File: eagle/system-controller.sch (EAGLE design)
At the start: 226 parts, among them J1 1, Q1 MOSFET-P-N-PAIR, Q10 MOSFET-P-N-PAIR, Q11 DNP/NTR4101P, Q2 MOSFET-P-N-PAIR, Q3 DON3035L, Q4 MOSFET-P-N-PAIR, Q5 MOSFET-P-N-PAIR, Q6 MOSFET-P-N-PAIR, Q7 MOSFET-P-N-PAIR, Q8 MOSFET-P-N-PAIR, Q9 DNP/NTR4101P, U1 TPS25944LRVCRWQFN-20-3X4, U10 TPS25944LRVCRWQFN-20-3X4, U11 ACPL-M61L, U12 ACPL-M61L, U13 TPS25944LRVCRWQFN-20-3X4, U14 ACPL-M61L, U15 ACPL-M61L, U2 LP5907MFX-3.0, U3 TPS25944LRVCRWQFN-20-3X4, U4 TPS25944LRVCRWQFN-20-3X4, U5 TPS25944LRVCRWQFN-20-3X4, U6 TPS25944LRVCRWQFN-20-3X4, U7 ATMEGA128L-8A(U/N), U8 TS4100, U9 TPS25944LRVCRWQFN-20-3X4, X1 8 MHz CRYSTAL-ABRACON-ABM3-SMD

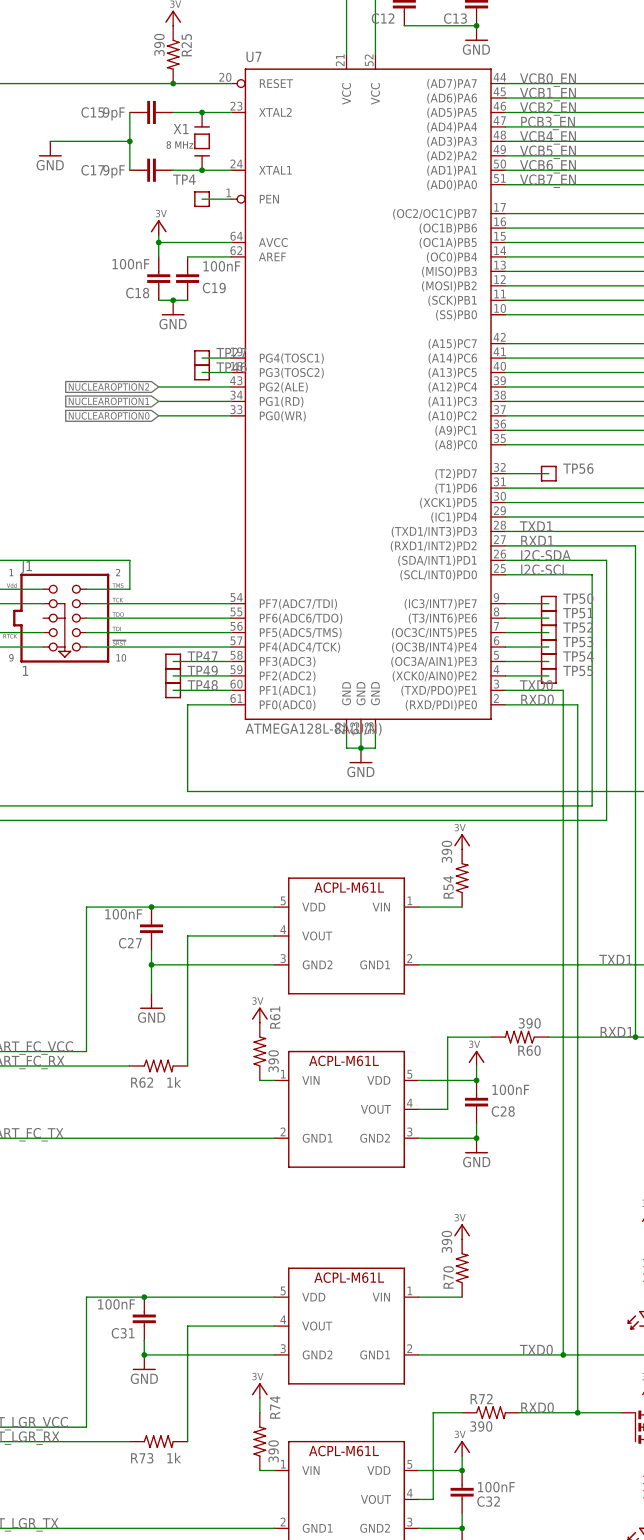
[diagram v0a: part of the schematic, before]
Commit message: Updating resitor and capacitor names
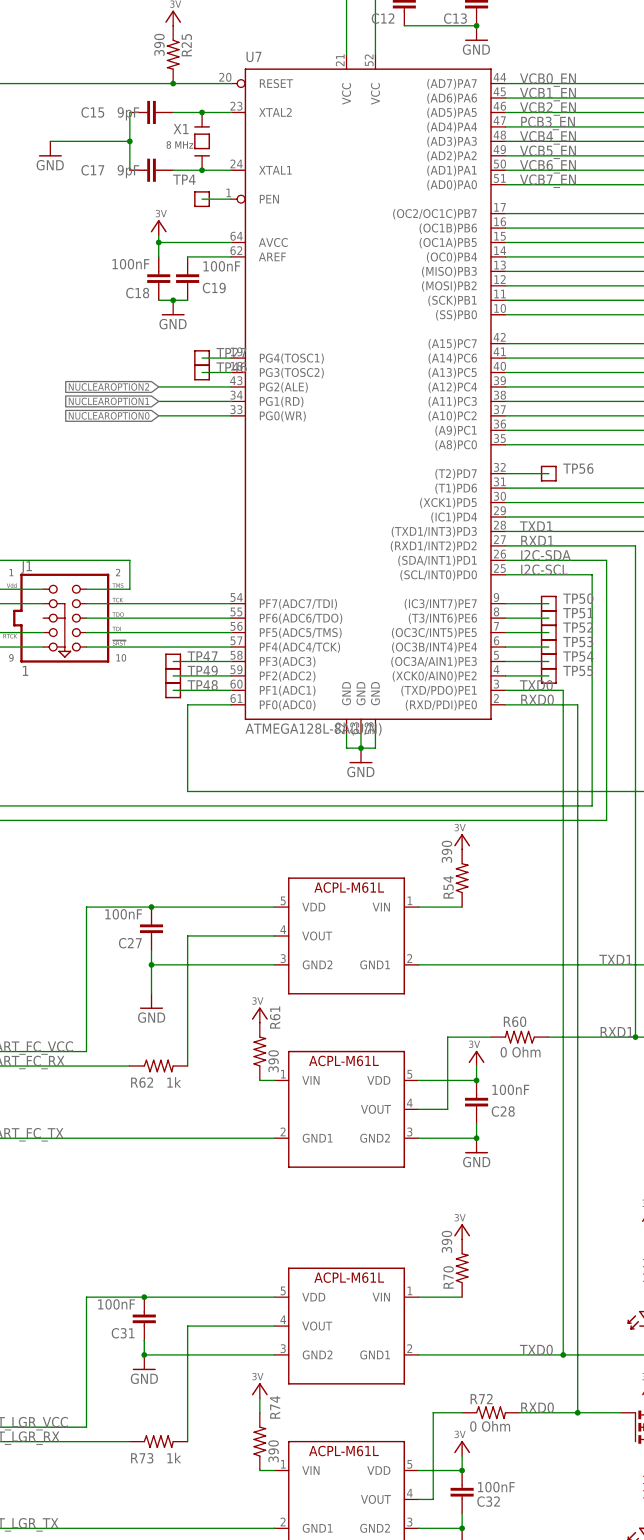
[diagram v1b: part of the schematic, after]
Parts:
- R60, R72: value 390 -> 0 Ohm
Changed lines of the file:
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@@
 <attribute name="MPN" value="C0603C104J4RACTU"/>
 </part>
-<part name="R60" library="rcl_custom" deviceset="R-US_" device="0603-B-NOSILK" value="390">
+<part name="R60" library="rcl_custom" deviceset="R-US_" device="0603-B-NOSILK" value="0 Ohm">
 <attribute name="DIST" value="digikey"/>
 <attribute name="DPN" value="A103093CT-ND"/>
@@
 <attribute name="MPN" value="4-1676481-5"/>
 </part>
-<part name="R72" library="rcl_custom" deviceset="R-US_" device="0603-B-NOSILK" value="390">
+<part name="R72" library="rcl_custom" deviceset="R-US_" device="0603-B-NOSILK" value="0 Ohm">
 <attribute name="DIST" value="digikey"/>
 <attribute name="DPN" value="A103093CT-ND"/>
@@
 <instance part="C15" gate="CE" x="139.7" y="264.16" smashed="yes" rot="R90">
 <attribute name="NAME" x="128.524" y="263.271" size="1.778" layer="95"/>
-<attribute name="VALUE" x="132.334" y="263.271" size="1.778" layer="96"/>
+<attribute name="VALUE" x="134.874" y="263.271" size="1.778" layer="96"/>
 <attribute name="DIST" x="139.7" y="264.16" size="1.778" layer="96" rot="R90" display="off"/>
 <attribute name="DPN" x="139.7" y="264.16" size="1.778" layer="96" rot="R90" display="off"/>
@@
 <instance part="C17" gate="CE" x="139.7" y="254" smashed="yes" rot="R90">
 <attribute name="NAME" x="128.524" y="253.111" size="1.778" layer="95"/>
-<attribute name="VALUE" x="132.334" y="253.111" size="1.778" layer="96"/>
+<attribute name="VALUE" x="134.874" y="253.111" size="1.778" layer="96"/>
 <attribute name="DIST" x="139.7" y="254" size="1.778" layer="96" rot="R90" display="off"/>
 <attribute name="DPN" x="139.7" y="254" size="1.778" layer="96" rot="R90" display="off"/>
@@
 <attribute name="VALUE" x="200.66" y="91.44" size="1.778" layer="96"/>
 </instance>
-<instance part="R60" gate="R" x="205.74" y="101.6" rot="R180">
+<instance part="R60" gate="R" x="205.74" y="101.6" smashed="yes" rot="R180">
 <attribute name="DIST" x="205.74" y="101.6" size="1.778" layer="96" rot="R180" display="off"/>
 <attribute name="DPN" x="205.74" y="101.6" size="1.778" layer="96" rot="R180" display="off"/>
 <attribute name="MFN" x="205.74" y="101.6" size="1.778" layer="96" rot="R180" display="off"/>
 <attribute name="MPN" x="205.74" y="101.6" size="1.778" layer="96" rot="R180" display="off"/>
+<attribute name="NAME" x="207.01" y="105.1814" size="1.778" layer="95" rot="R180"/>
+<attribute name="VALUE" x="209.55" y="99.822" size="1.778" layer="96" rot="R180"/>
 </instance>
 <instance part="R54" gate="R" x="195.58" y="129.54" smashed="yes" rot="R90">

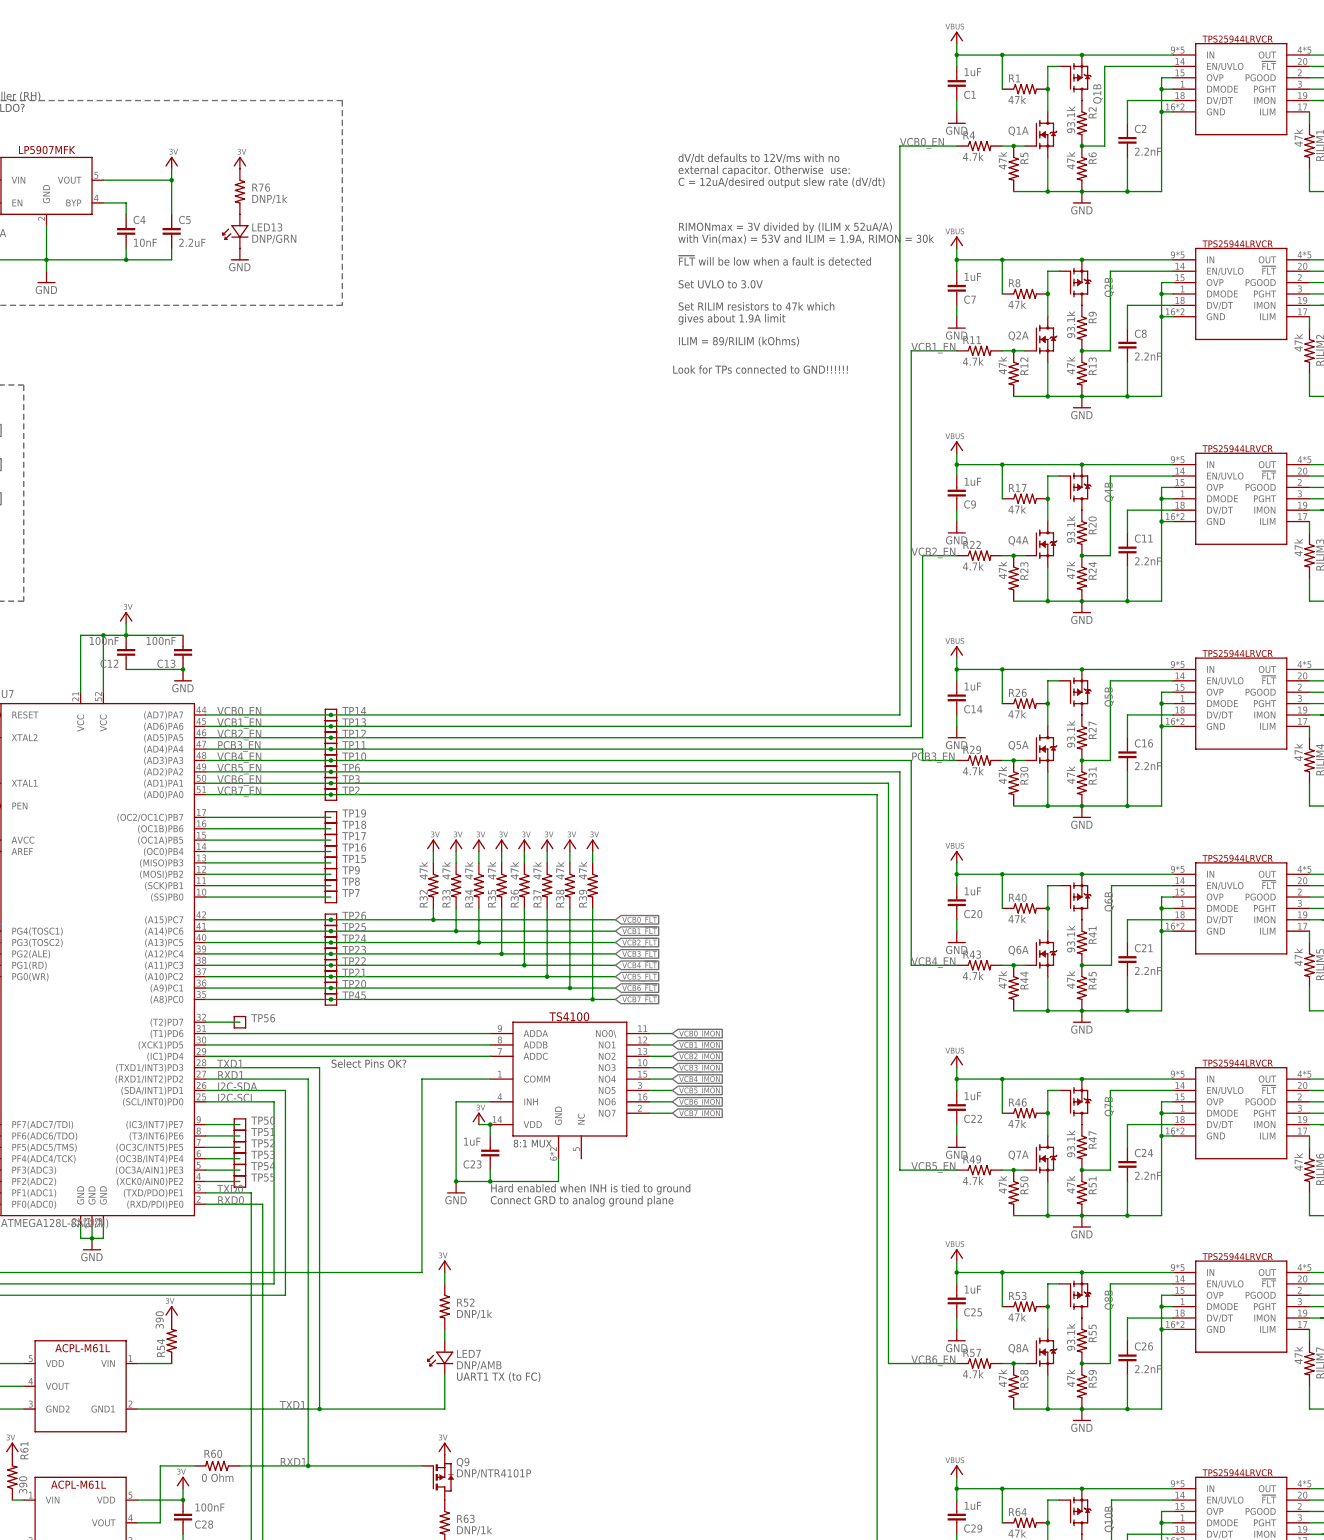
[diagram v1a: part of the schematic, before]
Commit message: added missing datasheets
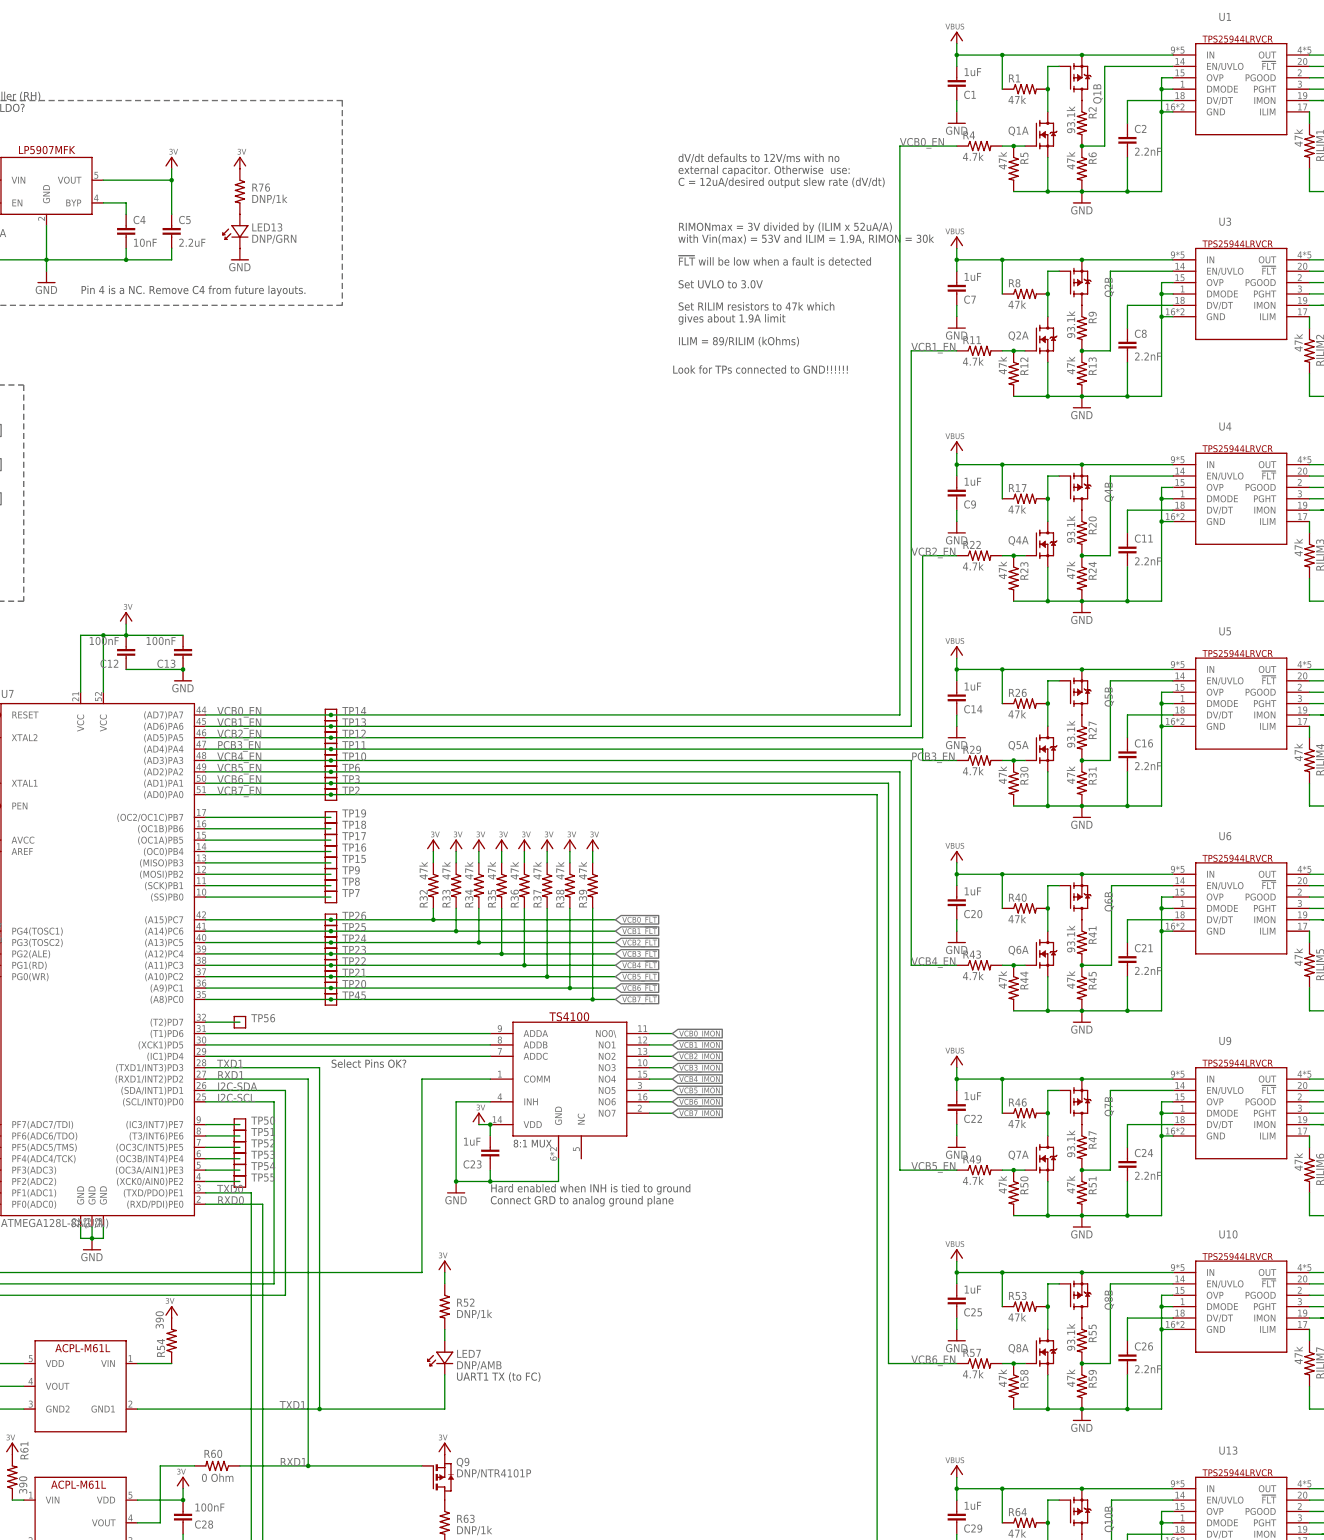
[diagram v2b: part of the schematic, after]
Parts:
- C11, C16, C2, C21, C24, C26, C30, C8: DIST (none) -> digikey; DPN (none) -> 1276-2239-1-ND; MFN (none) -> Samsung; MPN (none) -> CL10C222GA8NNNC
- D1, D2, D3: DIST (none) -> digikey; DPN (none) -> SSC53L-E3/57TGICT-ND; MFN (none) -> Vishay; MPN (none) -> SSC53L-E3/57T
- Q3: DIST (none) -> digikey; DPN (none) -> DMN62D0U-13DICT-ND; MFN (none) -> Diodes Inc.; MPN (none) -> DMN62D0U-13
- R18: DIST (none) -> digikey; DPN (none) -> 1276-4902-1-ND; MFN (none) -> Samsung; MPN (none) -> RC1608F474CS
- RIMON1, RIMON2, RIMON3, RIMON4, RIMON5, RIMON6, RIMON7, RIMON8: DIST (none) -> digikey; DPN (none) -> 1276-4787-1-ND; MFN (none) -> Samsung; MPN (none) -> RC1608F3012CS
- U1, U10, U13, U3, U4, U5, U6, U9: DIST (none) -> digikey; DPN (none) -> 296-42152-1-ND; MFN (none) -> Texas Instruments; MPN (none) -> TPS25944LRVCR
- U11, U12, U14, U15: DIST (none) -> digikey; DPN (none) -> 516-2169-5-ND; MFN (none) -> Broadcom; MPN (none) -> ACPL-M61L-000E
- U2: DIST (none) -> digikey; DPN (none) -> 296-40357-1-ND; MFN (none) -> Texas Inst.; MPN (none) -> LP5907MFX-3.0/NOPB
- U8: DIST (none) -> digikey; DPN (none) -> 336-3600-ND; MFN (none) -> Silicon Labs; MPN (none) -> TS4100ITQ1633
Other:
- note added: "Pin 4 is a NC. Remove C4 from future layouts."
